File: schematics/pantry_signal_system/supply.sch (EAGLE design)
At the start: 58 parts, among them J1 USBASP_PIN, J2 JST-XH254-3P, J3 JST-XH254-2P, J4 JST-XH254-2P, Q1 FDS4935A, Q2 FDS4935A, Q3 FDS4935A, U1 NC7WZ04, U2 AD8544SO-14, U3 FAN73611, U4 FAN73611, U5 MCP1703T-5002E/CB, U6 MCP1703T-5002E/CB, U7 MCP1703T-3302E/CB, U8 FAN73611, U9 ATTINY13SO-8

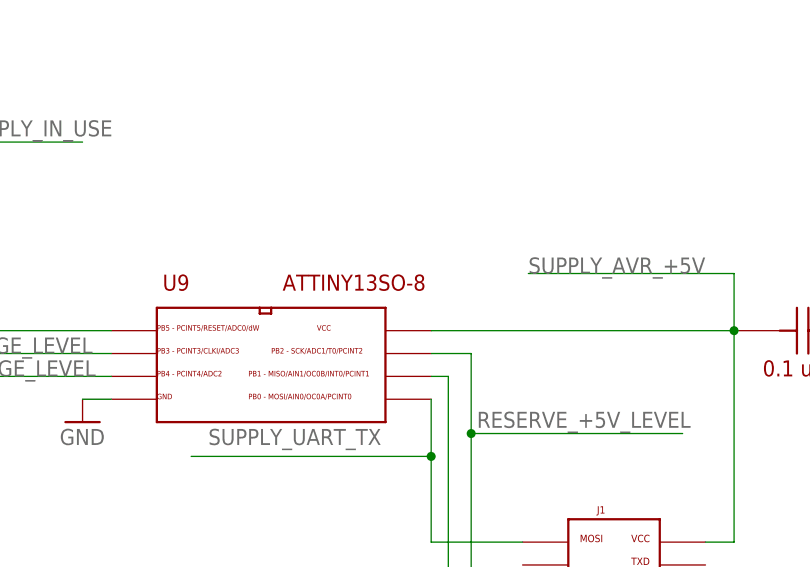
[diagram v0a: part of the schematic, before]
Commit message: Boards checked, some packages changed, library synced with this project
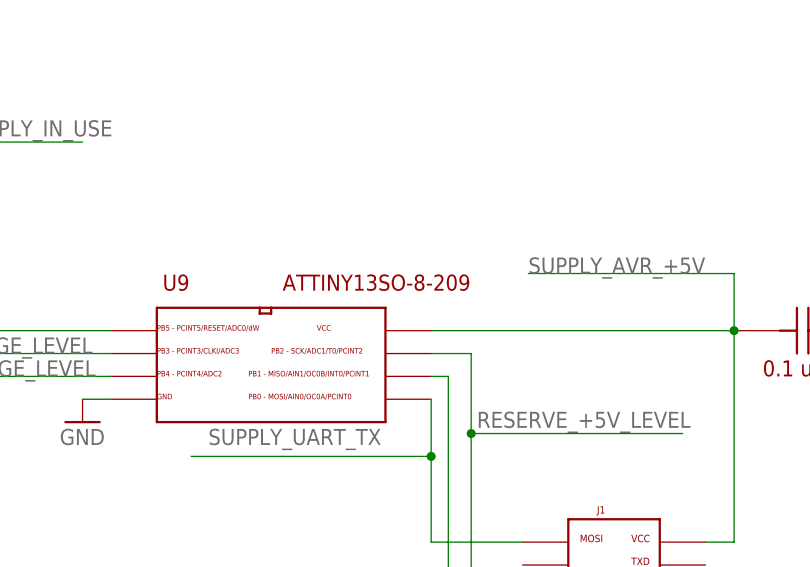
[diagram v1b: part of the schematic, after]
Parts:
- U9: value ATTINY13SO-8 -> ATTINY13SO-8-209; device my_devices:ATTINY13SO-8 -> my_devices:ATTINY13SO-8-209
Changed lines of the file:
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@@
 <setting verticaltext="up"/>
 </settings>
-<grid distance="0.05" unitdist="inch" unit="inch" style="lines" multiple="1" display="no" altdistance="0.01" altunitdist="inch" altunit="inch"/>
+<grid distance="0.1" unitdist="inch" unit="inch" style="lines" multiple="1" display="no" altdistance="0.01" altunitdist="inch" altunit="inch"/>
 <layers>
-<layer number="1" name="Top" color="4" fill="1" visible="no" active="no"/>
-<layer number="2" name="Route2" color="1" fill="3" visible="no" active="no"/>
-<layer number="3" name="Route3" color="4" fill="3" visible="no" active="no"/>
-<layer number="4" name="Route4" color="1" fill="4" visible="no" active="no"/>
-<layer number="5" name="Route5" color="4" fill="4" visible="no" active="no"/>
-<layer number="6" name="Route6" color="1" fill="8" visible="no" active="no"/>
-<layer number="7" name="Route7" color="4" fill="8" visible="no" active="no"/>
-<layer number="8" name="Route8" color="1" fill="2" visible="no" active="no"/>
-<layer number="9" name="Route9" color="4" fill="2" visible="no" active="no"/>
-<layer number="10" name="Route10" color="1" fill="7" visible="no" active="no"/>
-<layer number="11" name="Route11" color="4" fill="7" visible="no" active="no"/>
-<layer number="12" name="Route12" color="1" fill="5" visible="no" active="no"/>
-<layer number="13" name="Route13" color="4" fill="5" visible="no" active="no"/>
-<layer number="14" name="Route14" color="1" fill="6" visible="no" active="no"/>
-<layer number="15" name="Route15" color="4" fill="6" visible="no" active="no"/>
-<layer number="16" name="Bottom" color="1" fill="1" visible="no" active="no"/>
-<layer number="17" name="Pads" color="2" fill="1" visible="no" active="no"/>
-<layer number="18" name="Vias" color="2" fill="1" visible="no" active="no"/>
-<layer number="19" name="Unrouted" color="6" fill="1" visible="no" active="no"/>
-<layer number="20" name="Dimension" color="24" fill="1" visible="no" active="no"/>
-<layer number="21" name="tPlace" color="7" fill="1" visible="no" active="no"/>
-<layer number="22" name="bPlace" color="7" fill="1" visible="no" active="no"/>
-<layer number="23" name="tOrigins" color="15" fill="1" visible="no" active="no"/>
-<layer number="24" name="bOrigins" color="15" fill="1" visible="no" active="no"/>
-<layer number="25" name="tNames" color="7" fill="1" visible="no" active="no"/>
-<layer number="26" name="bNames" color="7" fill="1" visible="no" active="no"/>
-<layer number="27" name="tValues" color="7" fill="1" visible="no" active="no"/>
-<layer number="28" name="bValues" color="7" fill="1" visible="no" active="no"/>
+<layer number="1" name="Top" color="4" fill="1" visible="yes" active="no"/>
+<layer number="2" name="Route2" color="16" fill="1" visible="yes" active="no"/>
+<layer number="3" name="Route3" color="17" fill="1" visible="yes" active="no"/>
+<layer number="4" name="Route4" color="18" fill="1" visible="yes" active="no"/>
+<layer number="5" name="Route5" color="19" fill="1" visible="yes" active="no"/>
+<layer number="6" name="Route6" color="25" fill="1" visible="yes" active="no"/>
+<layer number="7" name="Route7" color="26" fill="1" visible="yes" active="no"/>
+<layer number="8" name="Route8" color="27" fill="1" visible="yes" active="no"/>
+<layer number="9" name="Route9" color="28" fill="1" visible="yes" active="no"/>
+<layer number="10" name="Route10" color="29" fill="1" visible="yes" active="no"/>
+<layer number="11" name="Route11" color="30" fill="1" visible="yes" active="no"/>
+<layer number="12" name="Route12" color="20" fill="1" visible="yes" active="no"/>
+<layer number="13" name="Route13" color="21" fill="1" visible="yes" active="no"/>
+<layer number="14" name="Route14" color="22" fill="1" visible="yes" active="no"/>
+<layer number="15" name="Route15" color="23" fill="1" visible="yes" active="no"/>
+<layer number="16" name="Bottom" color="1" fill="1" visible="yes" active="no"/>
+<layer number="17" name="Pads" color="2" fill="1" visible="yes" active="no"/>
+<layer number="18" name="Vias" color="2" fill="1" visible="yes" active="no"/>
+<layer number="19" name="Unrouted" color="6" fill="1" visible="yes" active="no"/>
+<layer number="20" name="Dimension" color="24" fill="1" visible="yes" active="no"/>
+<layer number="21" name="tPlace" color="7" fill="1" visible="yes" active="no"/>
+<layer number="22" name="bPlace" color="7" fill="1" visible="yes" active="no"/>
+<layer number="23" name="tOrigins" color="15" fill="1" visible="yes" active="no"/>
+<layer number="24" name="bOrigins" color="15" fill="1" visible="yes" active="no"/>
+<layer number="25" name="tNames" color="7" fill="1" visible="yes" active="no"/>
+<layer number="26" name="bNames" color="7" fill="1" visible="yes" active="no"/>
+<layer number="27" name="tValues" color="7" fill="1" visible="yes" active="no"/>
+<layer number="28" name="bValues" color="7" fill="1" visible="yes" active="no"/>
 <layer number="29" name="tStop" color="7" fill="3" visible="no" active="no"/>
 <layer number="30" name="bStop" color="7" fill="6" visible="no" active="no"/>
@@
 <layer number="35" name="tGlue" color="7" fill="4" visible="no" active="no"/>
 <layer number="36" name="bGlue" color="7" fill="5" visible="no" active="no"/>
-<layer number="37" name="tTest" color="7" fill="1" visible="no" active="no"/>
-<layer number="38" name="bTest" color="7" fill="1" visible="no" active="no"/>
+<layer number="37" name="tTest" color="7" fill="1" visible="yes" active="no"/>
+<layer number="38" name="bTest" color="7" fill="1" visible="yes" active="no"/>
 <layer number="39" name="tKeepout" color="4" fill="11" visible="no" active="no"/>
 <layer number="40" name="bKeepout" color="1" fill="11" visible="no" active="no"/>
@@
 <layer number="44" name="Drills" color="7" fill="1" visible="no" active="no"/>
 <layer number="45" name="Holes" color="7" fill="1" visible="no" active="no"/>
-<layer number="46" name="Milling" color="3" fill="1" visible="no" active="no"/>
-<layer number="47" name="Measures" color="7" fill="1" visible="no" active="no"/>
-<layer number="48" name="Document" color="7" fill="1" visible="no" active="no"/>
-<layer number="49" name="Reference" color="7" fill="1" visible="no" active="no"/>
-<layer number="51" name="tDocu" color="7" fill="1" visible="no" active="no"/>
-<layer number="52" name="bDocu" color="7" fill="1" visible="no" active="no"/>
+<layer number="46" name="Milling" color="3" fill="1" visible="yes" active="no"/>
+<layer number="47" name="Measures" color="7" fill="1" visible="yes" active="no"/>
+<layer number="48" name="Document" color="7" fill="1" visible="yes" active="no"/>
+<layer number="49" name="Reference" color="7" fill="1" visible="yes" active="no"/>
+<layer number="51" name="tDocu" color="7" fill="1" visible="yes" active="no"/>
+<layer number="52" name="bDocu" color="7" fill="1" visible="yes" active="no"/>
 <layer number="88" name="SimResults" color="9" fill="1" visible="yes" active="yes"/>
 <layer number="89" name="SimProbes" color="9" fill="1" visible="yes" active="yes"/>
@@
 <part name="J4" library="my_devices" deviceset="JST-XH254-2P" device=""/>
 <part name="GND32" library="supply1" library_urn="urn:adsk.eagle:library:371" deviceset="GND" device=""/>
-<part name="U9" library="my_devices" deviceset="ATTINY13" device="SO-8" value="ATTINY13SO-8"/>
+<part name="U9" library="my_devices" deviceset="ATTINY13" device="SO-8-209" value="ATTINY13SO-8-209"/>
 <part name="GND13" library="supply1" library_urn="urn:adsk.eagle:library:371" deviceset="GND" device=""/>
 <part name="FU1" library="my_devices" deviceset="FU" device="" value="H520PT / 1A"/>

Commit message: 1. Fixed issues in boards and firmwares
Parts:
- R1, R2, R5: device my_devices:RD3296-Z -> my_devices:RD3296W-1-205LF
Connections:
- net +12V: now also J4.PIN2; no longer J4.PIN1
- net GND: now also J4.PIN1; no longer J4.PIN2
